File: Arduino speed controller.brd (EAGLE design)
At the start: 53.3 x 59.7 mm, 14 parts, among them J1 AUDIO-JACK2KIT, J2 AUDIO-JACK2KIT

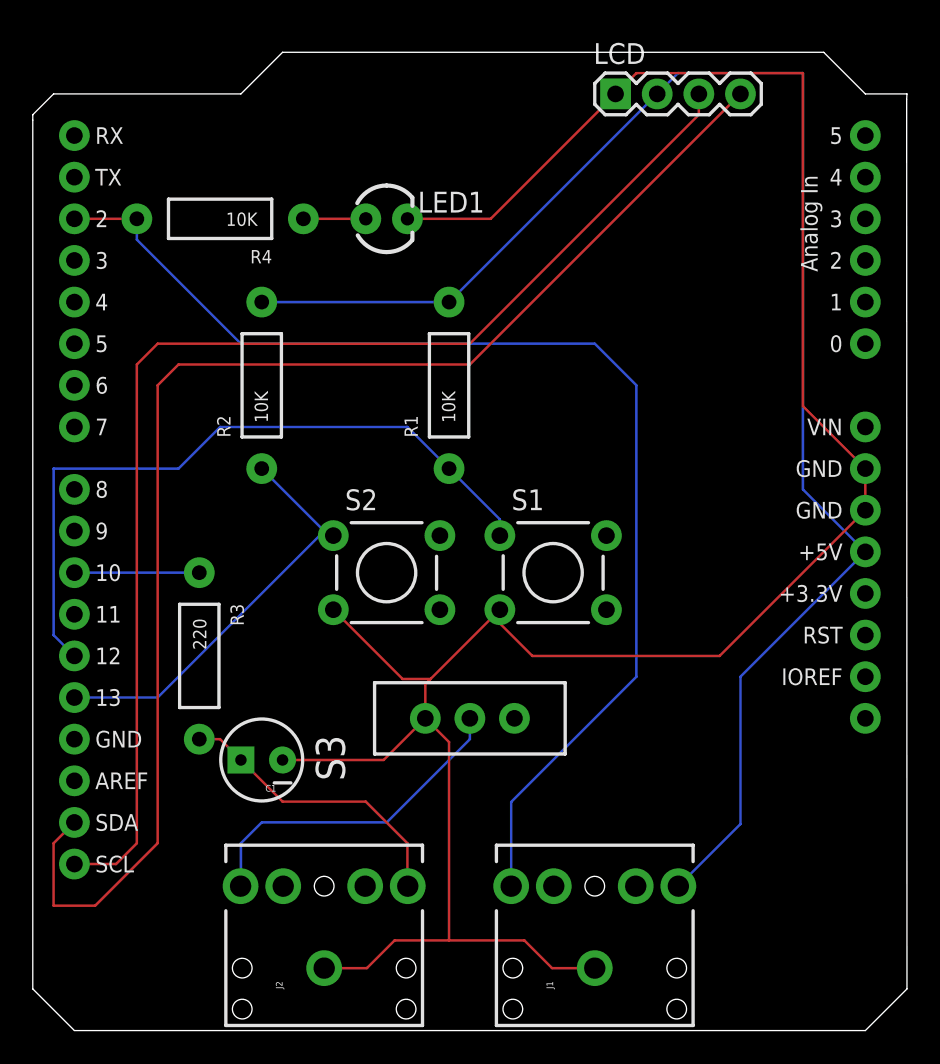
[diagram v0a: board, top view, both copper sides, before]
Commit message: Copper fills (disabled), moved jacks
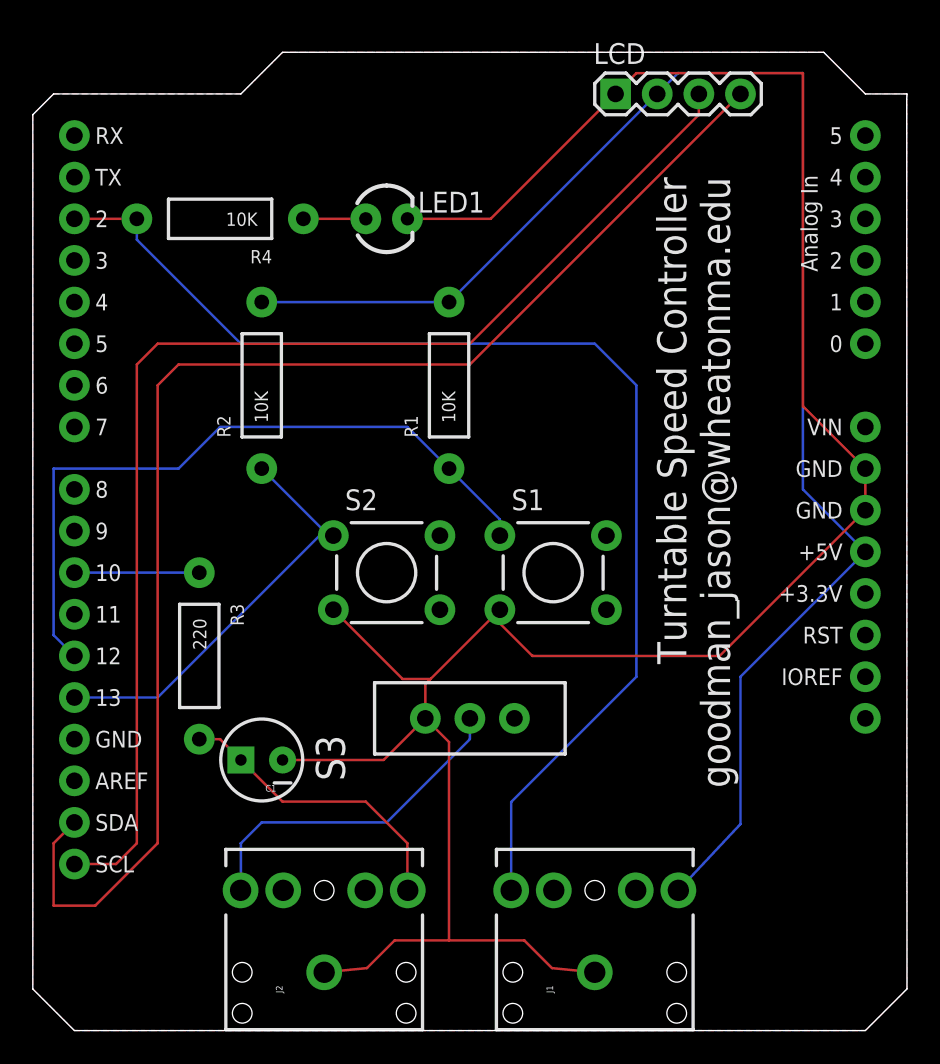
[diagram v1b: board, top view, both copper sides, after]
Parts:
- removed FRAME1: FRAME-LETTER, SparkFun-Aesthetics:CREATIVE_COMMONS
- S2: value Faster -> Slower
- moved J1 0.25 mm to (34.3, 3.56)
- moved J2 0.25 mm to (17.8, 3.56)
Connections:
- net FASTER: now also R1.P$1, S1.1, U$1.D12; no longer R2.P$1, S2.1, U$1.D13
- net SLOWER: now also R2.P$1, S2.1, U$1.D13; no longer R1.P$1, S1.1, U$1.D12
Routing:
- net SLOWER: track 43.6 -> 25.6 mm
- net FASTER: track 25.6 -> 43.6 mm
- added copper zone on layer 1, net GND
- added copper zone on layer 16, net GND
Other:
- outline, holes or cut-outs redrawn
- board text added: "Turntable Speed Controller goodman_jason@wheatonma.edu"

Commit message: Added DAC
Added DAC
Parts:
- removed C1: 10uF, SparkFun-Passives:CPOL-RADIAL-10UF-25V
- added DAC: (no value), SparkFun-Connectors:1X06
- S1: value Slower -> Faster
- S3: value (none) -> MHS122K; device SparkFun-Electromechanical:SWITCH-SPDT_KIT -> switches:APEM-MHS122K
- moved R3 33.9 mm to (43.2, 15.2), turned to 180 degrees
- turned S3 to 180 degrees
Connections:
- removed net N$4: C1.1, J2.TIP, R3.P$2
- removed net SPEEDCTRL: R3.P$1, U$1.D10
- new net N$1: J2.RING, S3.CMN
- new net N$3: DAC.6, J2.TIP
- net 5V: now also DAC.1
- net CLK: now also DAC.3
- net DAT: now also DAC.4
- net FASTER: now also U$1.D11; no longer U$1.D12
- net GND: now also DAC.2, R3.P$1; no longer C1.2, S3.1
- net N$2: now also R3.P$2, S3.1; no longer J2.RING, S3.2
- net SLOWER: now also U$1.D12; no longer U$1.D13
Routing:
- net N$3: track 0.00 -> 44.4 mm
- net DAT: track 84.4 -> 102.7 mm
- net N$4: track 18.2 -> 0.00 mm
- net N$1: track 0.00 -> 17.8 mm
- net CLK: track 75.4 -> 92.7 mm
- net N$2: track 20.8 -> 9.23 mm
- net SPEEDCTRL: track 7.62 -> 0.00 mm
- net SLOWER: track 25.6 -> 22.7 mm
- net 5V: track 94.9 -> 97.7 mm
- net FASTER: track 43.6 -> 41.0 mm
- net GND: track 141.7 -> 144.1 mm
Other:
- board text added: "goodman_jason@wheatonma.edu Turntable Speed Controller 1.0"
- board text removed: "Turntable Speed Controller goodman_jason@wheatonma.edu"
